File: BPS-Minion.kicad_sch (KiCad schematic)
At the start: 7 parts, among them J5 SOMConnector

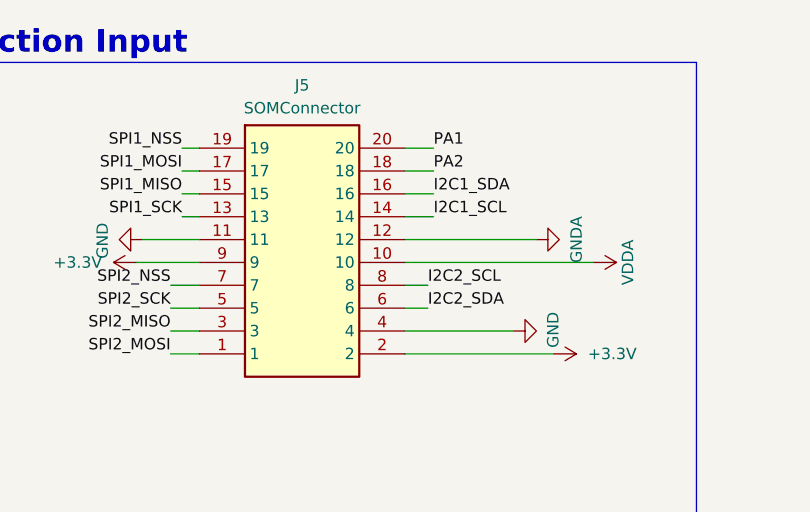
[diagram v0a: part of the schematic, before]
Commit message: power flags
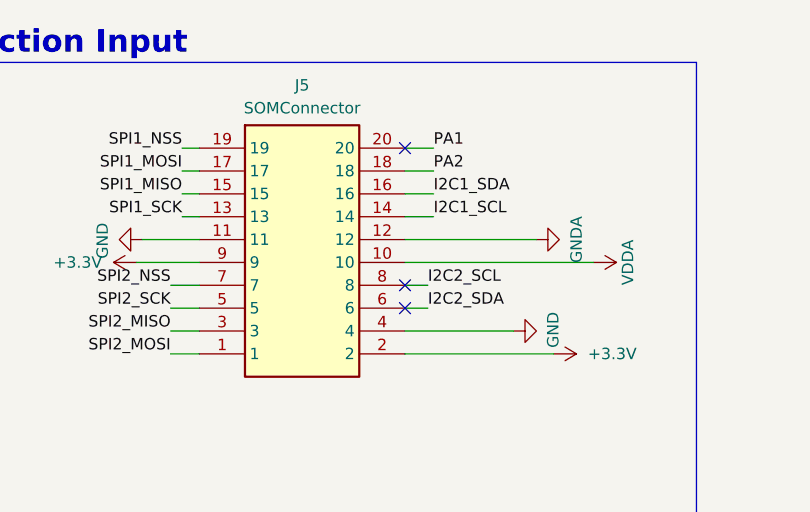
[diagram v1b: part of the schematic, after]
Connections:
- no-connect marks 0 -> 3
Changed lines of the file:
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@@
 (kicad_sch (version 20230121) (generator eeschema)
   (paper "A4")
+  (no_connect (at 247.65 51.435))
+  (no_connect (at 247.65 48.895))
+  (no_connect (at 247.65 33.655))
   (wire (pts (xy 191.135 56.515) (xy 191.135 60.325))
     (stroke (width 0) (type default))

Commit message: bypass capacitors
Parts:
- added R85: 50, Resistor_SMD:R_0805_2012Metric, symbol Device:R_US
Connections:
- net SPI1_MOSI: now also R85.1; no longer J5.17
- new net: J5.17, R85.2
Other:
- moved on the sheet: J5

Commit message: define edge cuts for new volttemp
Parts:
- J5: footprint UTSVT_Connectors:Molex_52465-2070 -> UTSVT_Connectors:Molex_53307-2071
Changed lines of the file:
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@@
       (effects (font (size 1.27 1.27)))
     )
-    (property "Footprint" "UTSVT_Connectors:Molex_52465-2070" (at 247.65 131.75 0)
+    (property "Footprint" "UTSVT_Connectors:Molex_53307-2071" (at 247.65 131.75 0)
       (effects (font (size 1.27 1.27)) (justify left top) hide)
     )

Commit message: why so many bugs >:(
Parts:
- added C1: 10u, Capacitor_SMD:C_0805_2012Metric_Pad1.18x1.45mm_HandSolder, symbol Device:C
- added C2: 1u, Capacitor_SMD:C_0805_2012Metric_Pad1.18x1.45mm_HandSolder, symbol Device:C
- added U12: MIC5317-2.5xM5, Package_TO_SOT_SMD:SOT-23-5, symbol Regulator_Linear:MIC5317-2.5xM5
- renumbered D13 to D1, J5 to J1, R21 to R1, R85 to R2
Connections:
- net GNDA: now also C1.1, C2.2, U12.2 (GND)
- net VDDA: now also C1.2, U12.1 (VIN), U12.3 (EN)
- new net +2V5: C2.1, U12.5 (VOUT)
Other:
- note added: "2.5V Reference for ADC"

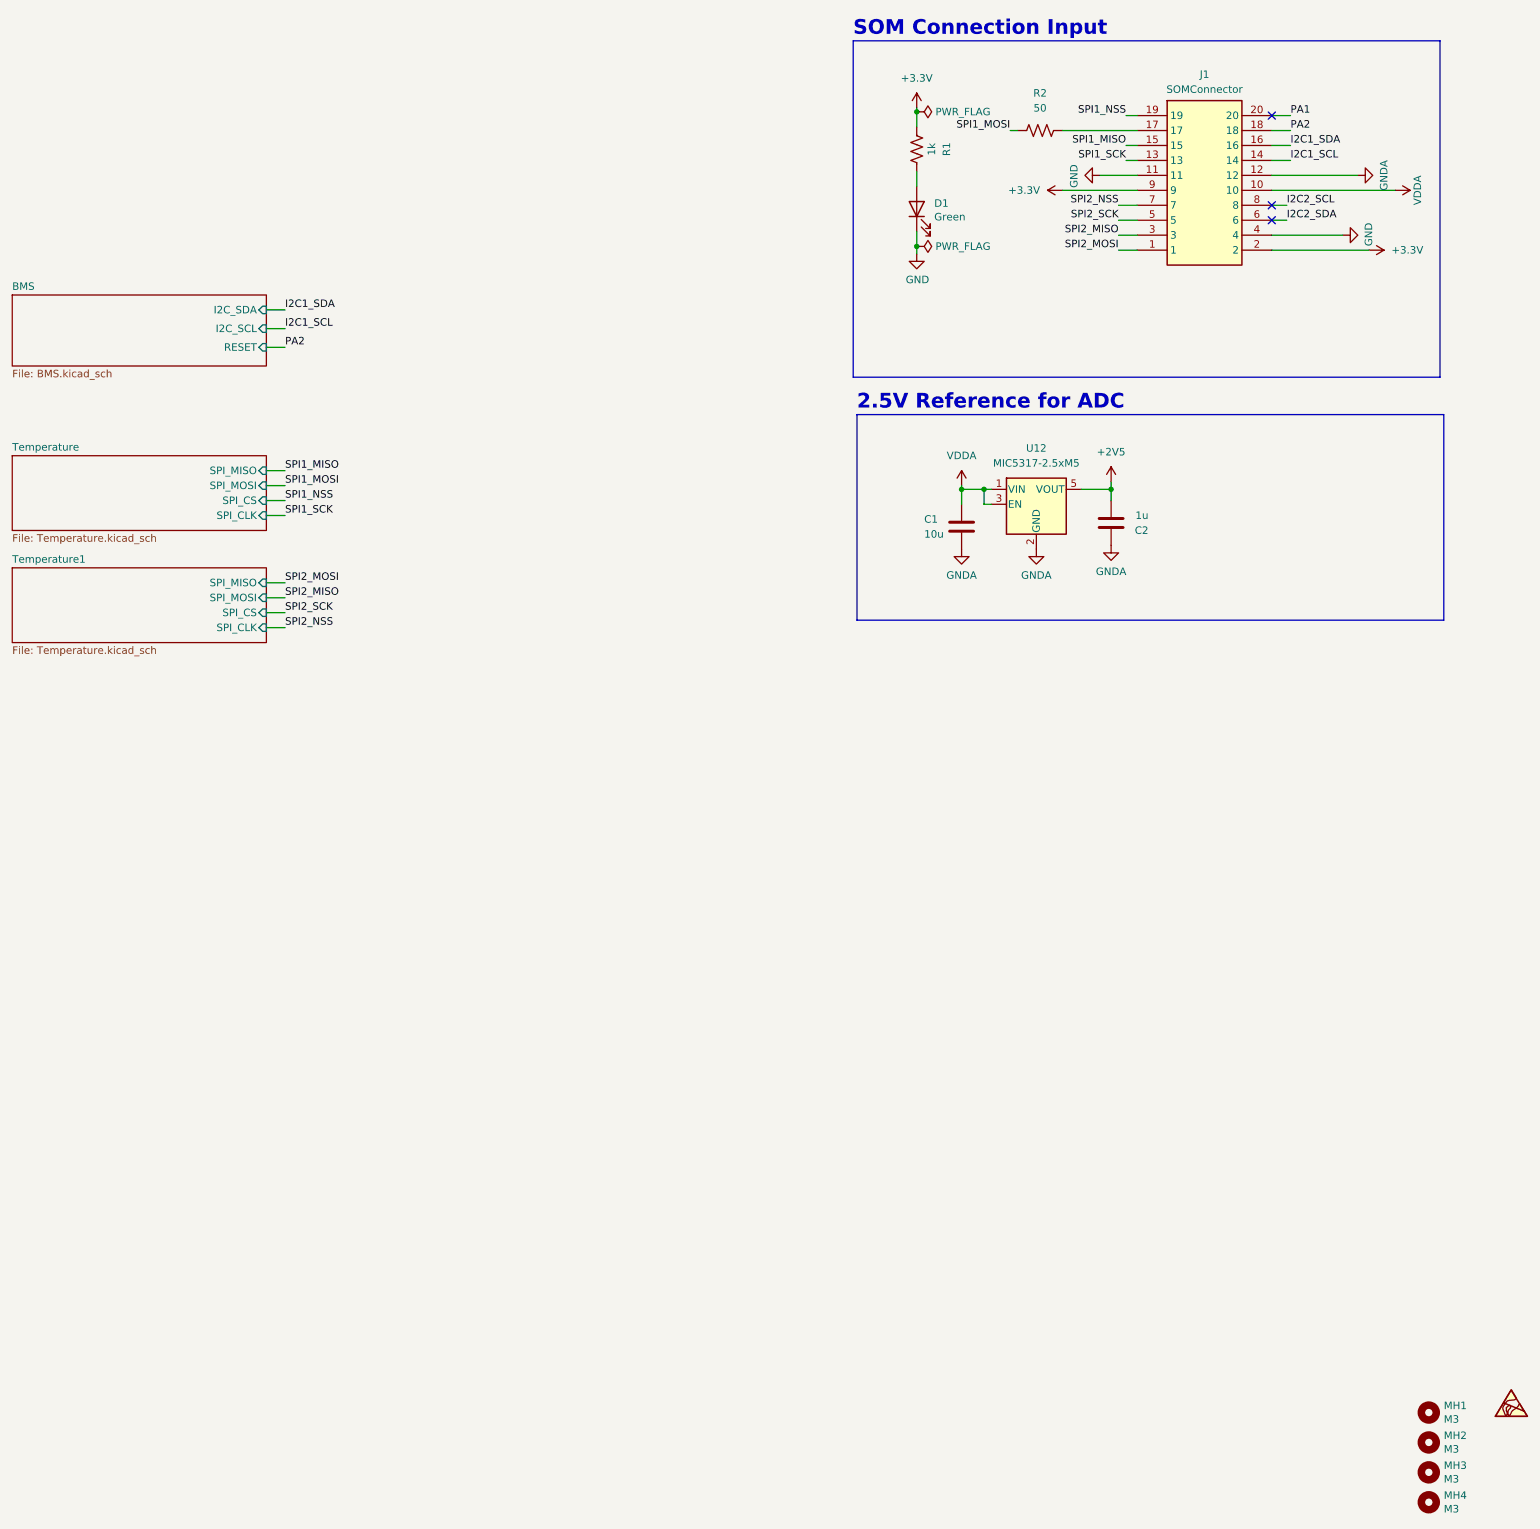
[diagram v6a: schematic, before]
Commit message: Use PeripheralSOM symbol
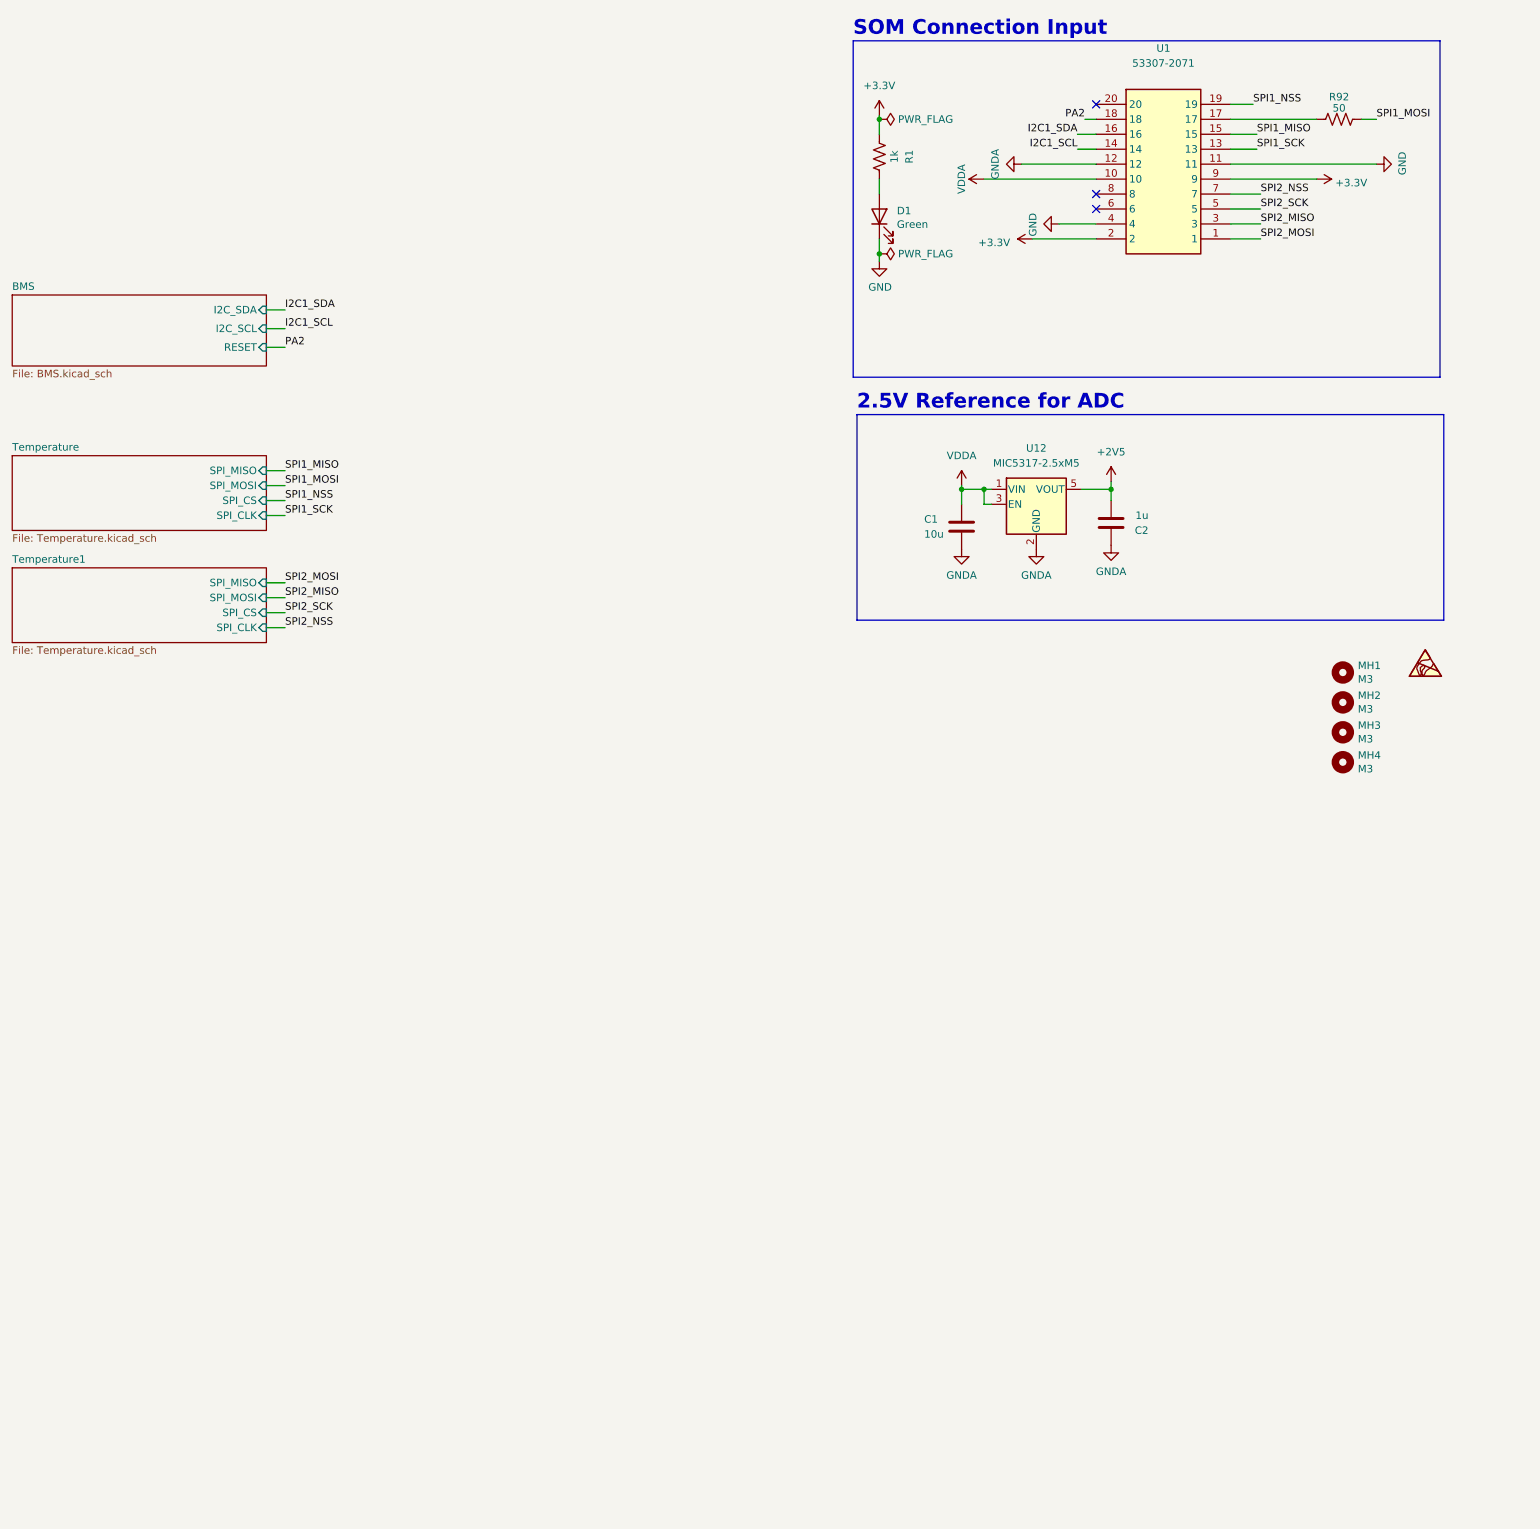
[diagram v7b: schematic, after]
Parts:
- removed J1: SOMConnector, UTSVT_Connectors:Molex_53307-2071, symbol utsvt-connectors:SOMConnector
- removed R2: 50, Resistor_SMD:R_0805_2012Metric, symbol Device:R_US
- added R92: 50, Resistor_SMD:R_0805_2012Metric, symbol Device:R_US
- added U1: ~, UTSVT_Special:PeripheralSOM, symbol utsvt-misc:PeripheralSOM
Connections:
- net +3.3V: now also U1.2, U1.9
- net GND: now also U1.11, U1.4
- net GNDA: now also U1.12
- net I2C1_SCL: now also U1.14
- net I2C1_SDA: now also U1.16
- net PA2: now also U1.18
- net SPI1_MISO: now also U1.15
- net SPI1_MOSI: now also R92.1
- net SPI1_NSS: now also U1.19
- net SPI1_SCK: now also U1.13
- net SPI2_MISO: now also U1.3
- net SPI2_MOSI: now also U1.1
- net SPI2_NSS: now also U1.7
- net SPI2_SCK: now also U1.5
- net VDDA: now also U1.10
- new net: R92.2, U1.17
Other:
- moved on the sheet: D1, MH1, MH2, MH3, MH4, R1

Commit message: time flies when you're kicadding :(
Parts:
- C1, C2: footprint Capacitor_SMD:C_0805_2012Metric_Pad1.18x1.45mm_HandSolder -> Capacitor_SMD:C_0805_2012Metric
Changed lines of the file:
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@@
       (effects (font (size 1.27 1.27)) (justify right))
     )
-    (property "Footprint" "Capacitor_SMD:C_0805_2012Metric_Pad1.18x1.45mm_HandSolder" (at 225.1202 109.855 0)
+    (property "Footprint" "Capacitor_SMD:C_0805_2012Metric" (at 225.1202 109.855 0)
       (effects (font (size 1.27 1.27)) hide)
     )
@@
       (effects (font (size 1.27 1.27)) (justify right))
     )
-    (property "Footprint" "Capacitor_SMD:C_0805_2012Metric_Pad1.18x1.45mm_HandSolder" (at 197.7898 102.87 0)
+    (property "Footprint" "Capacitor_SMD:C_0805_2012Metric" (at 197.7898 102.87 0)
       (effects (font (size 1.27 1.27)) hide)
     )
